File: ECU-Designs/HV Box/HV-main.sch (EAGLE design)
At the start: 62 parts, among them IC2 MCP6002, IC3 MCP6002, T1 120, T2 120, X1 MINIFIT_5566-8

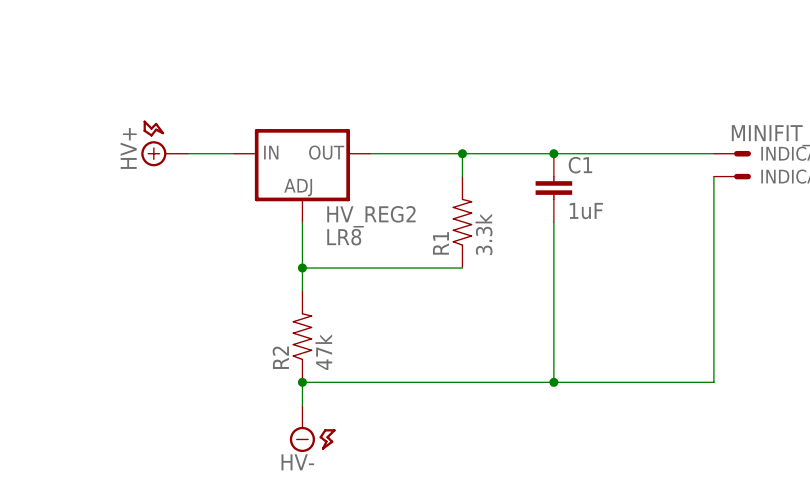
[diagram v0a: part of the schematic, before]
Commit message: Modify elcon charger schematic, fix LR8 values for accumulator indicator for FSAE
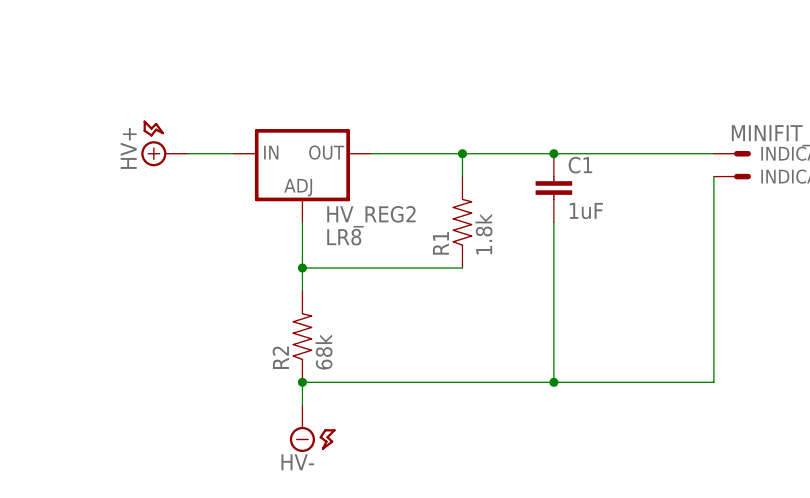
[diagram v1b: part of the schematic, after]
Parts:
- R1: value 3.3k -> 1.8k
- R2: value 47k -> 68k
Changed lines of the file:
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@@
 <?xml version="1.0" encoding="utf-8"?>
 <!DOCTYPE eagle SYSTEM "eagle.dtd">
-<eagle version="7.2.0">
+<eagle version="7.7.0">
 <drawing>
 <settings>
@@
 <setting verticaltext="up"/>
 </settings>
-<grid distance="0.1" unitdist="inch" unit="inch" style="lines" multiple="1" display="no" altdistance="0.05" altunitdist="inch" altunit="inch"/>
+<grid distance="0.1" unitdist="inch" unit="inch" style="lines" multiple="1" display="no" altdistance="0.01" altunitdist="inch" altunit="inch"/>
 <layers>
 <layer number="1" name="Top" color="4" fill="1" visible="no" active="no"/>
@@
 <part name="HV_REG2" library="HyTechDevices" deviceset="HV_LIN_REG_LR8" device="SMD" value="LR8"/>
 <part name="C1" library="HyTechDevices" deviceset="CAP" device="0805" value="1uF"/>
-<part name="R1" library="HyTechDevices" deviceset="RESISTOR" device="0805-RES" value="3.3k"/>
-<part name="R2" library="HyTechDevices" deviceset="RESISTOR" device="0805-RES" value="47k"/>
+<part name="R1" library="HyTechDevices" deviceset="RESISTOR" device="0805-RES" value="1.8k"/>
+<part name="R2" library="HyTechDevices" deviceset="RESISTOR" device="0805-RES" value="68k"/>
 <part name="INDICATOR" library="HyTechDevices" deviceset="MINIFIT_5566-2" device="" value="MINIFIT_5566-2"/>
 <part name="U$6" library="supply2" deviceset="HV+" device=""/>

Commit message: HV Board progress
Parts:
- removed C1, C2: 1uF, HyTechDevices:CAP0805
- removed F1, F2: 2.0, HyTechDevices:RESISTOR0805-RES
- removed FUSE+, FUSE-: 0751.0110_FUSE_CLIP, HyTechDevices:0751.0110_FUSE_CLIP
- removed R3: 6.8k, HyTechDevices:RESISTOR0805-RES
- removed TSMP: MINIFIT_5566-2, HyTechDevices:MINIFIT_5566-2
- removed TSMP_R+, TSMP_R-: 10K, 10w, HyTechDevices:RESISTOR10W
- added FUSE: 250mA, HyTechDevices:FUSE_MIDGET
- added R20: 6.8k, HyTechDevices:RESISTOR0805-RES
- added R21, R22: 500k, HyTechDevices:RESISTOR0805-RES
- added R23, R24: 40k, HyTechDevices:RESISTOR0805-RES
- R5: value 1.5m -> 500k
- R6: value 120k -> 40k
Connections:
- removed net HVIN-: F2.2, HVIN--1.S, HVIN--2.S
- removed net N$31: C2.2, HV_REG1.ADJ, R3.1, R4.2
- removed net N$38: TSMP-1.S, TSMP_R+.2
- removed net N$39: TSMP-2.S, TSMP_R-.2
- removed net N$6: F2.1, FUSE-.1
- removed net N$7: F1.1, FUSE+.1
- new net N$10: R21.1, R22.1
- new net N$11: R21.2, R5.2
- new net N$12: R23.1, R24.1
- new net N$13: R23.2, R6.2
- new net N$9: HV_REG1.ADJ, R20.1, R4.2
- net HV+: now also FUSE.P2, R22.2; no longer FUSE+.2, R5.2, TSMP_R+.1
- net HV-: now also HVIN--1.S, HVIN--2.S; no longer C1.2, FUSE-.2, TSMP_R-.1
- net HVIN+: now also FUSE.P1; no longer F1.2
- net N$1: no longer C1.1
- net N$2: now also R20.2; no longer C2.1, R3.2
- net N$36: now also R24.2; no longer R6.2
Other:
- note added: "IMD Connections"
- note removed: "1/8W 0805 Limiting to 250mA"
- note removed: "IMD & TSMP Connections"

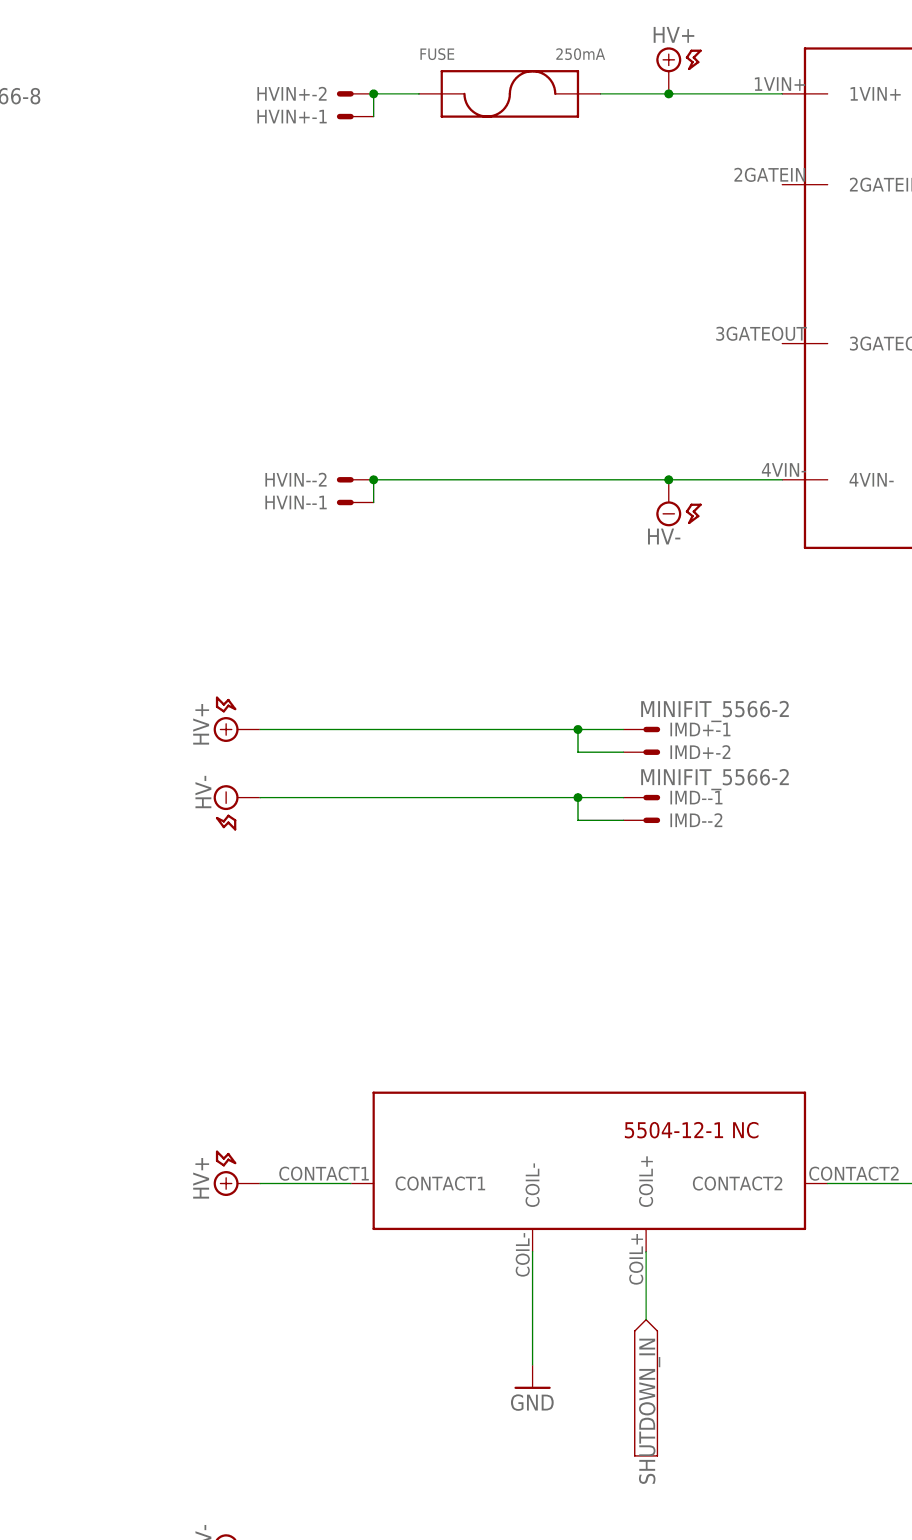
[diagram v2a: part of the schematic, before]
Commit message: Updated HV board and stuffs
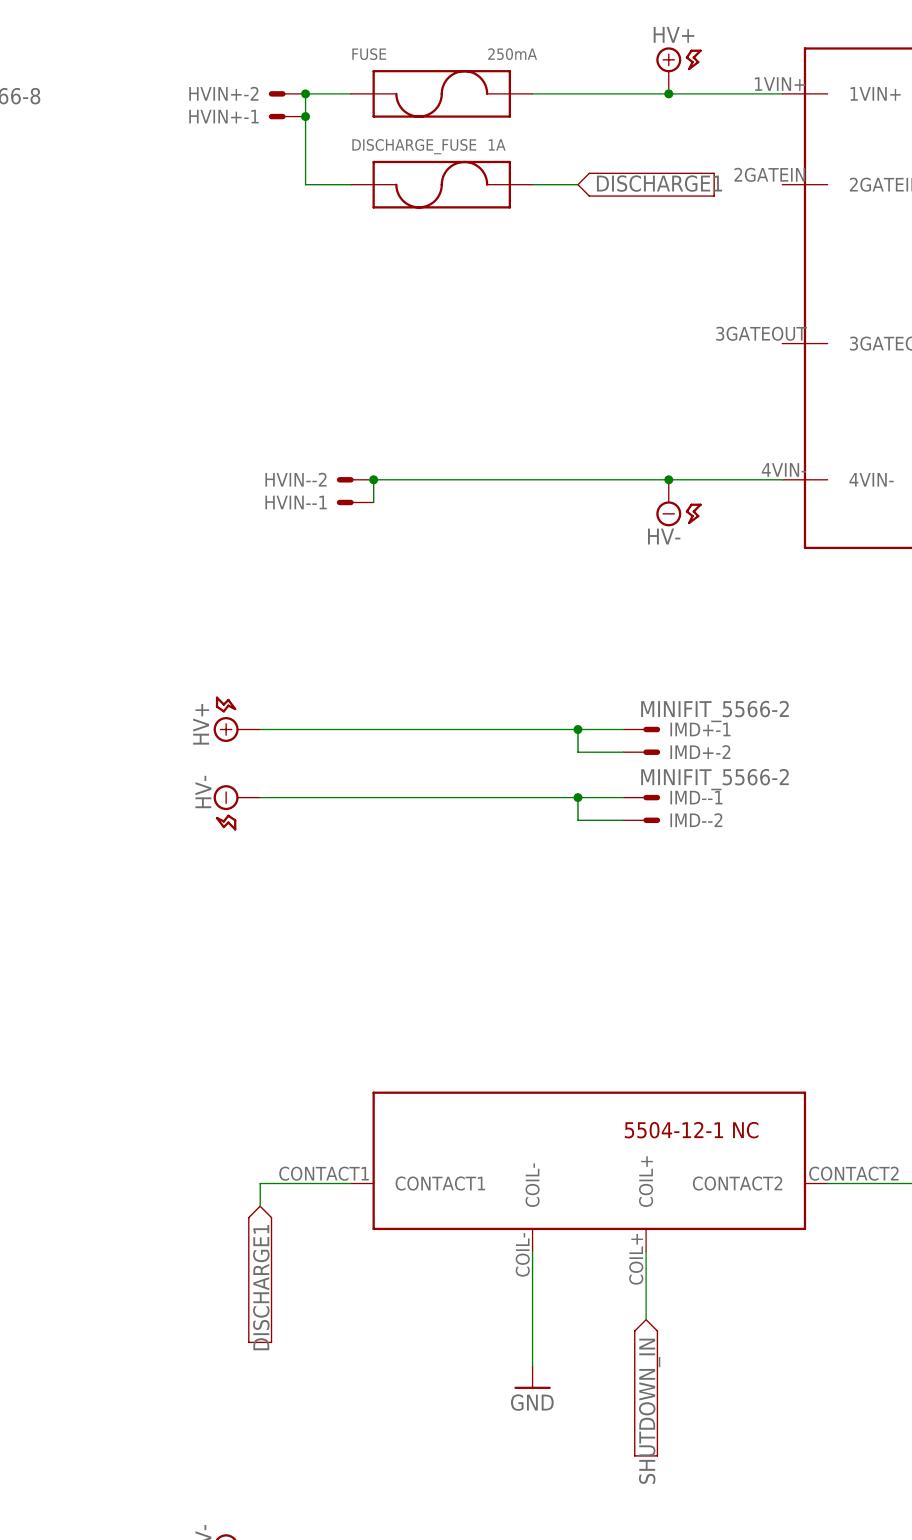
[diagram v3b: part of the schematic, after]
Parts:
- added DISCHARGE_FUSE: 1A, HyTechDevices:FUSE_5X20MM
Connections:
- net N$37 renamed DISCHARGE2
- new net BMS_OK: MAIN-2.S
- new net CHARGE_ENABLE: MAIN-3.S
- new net DISCHARGE1: DISCHARGE_FUSE.P2, U$12.CONTACT1
- net BSPD_CURRENT: now also MAIN-9.S
- net HV+: no longer U$12.CONTACT1
- net HVIN+: now also DISCHARGE_FUSE.P1
- net OKHS_OUT: now also MAIN-1.S
- net SHUTDOWN_IN: now also MAIN-10.S
- net TSAL+: now also MAIN-12.S
- net VDD: now also MAIN-11.S
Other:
- moved on the sheet: FUSE, HVIN+-1, HVIN+-2
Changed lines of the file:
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@@
 <?xml version="1.0" encoding="utf-8"?>
 <!DOCTYPE eagle SYSTEM "eagle.dtd">
-<eagle version="7.2.0">
+<eagle version="8.0.1">
 <drawing>
 <settings>
@@
 <part name="D1" library="HyTechDevices" deviceset="DIODE" device="0805" value=""/>
 <part name="D2" library="HyTechDevices" deviceset="DIODE" device="0805" value=""/>
-<part name="U$4" library="supply2" deviceset="HV+" device=""/>
 <part name="U$14" library="supply2" deviceset="HV-" device=""/>
 <part name="IC3" library="HyTechDevices" deviceset="MCP6002" device=""/>
@@
 <part name="R23" library="HyTechDevices" deviceset="RESISTOR" device="0805-RES" value="40k"/>
 <part name="R24" library="HyTechDevices" deviceset="RESISTOR" device="0805-RES" value="40k"/>
+<part name="SUPPLY17" library="supply2" deviceset="V&lt;--" device="" value="DISCHARGE1"/>
+<part name="DISCHARGE_FUSE" library="HyTechDevices" deviceset="FUSE" device="_5X20MM" value="1A"/>
+<part name="SUPPLY18" library="supply2" deviceset="V&lt;--" device="" value="DISCHARGE1"/>
 </parts>
 <sheets>
@@
 <instance part="SUPPLY1" gate="G$1" x="55.88" y="22.86"/>
 <instance part="SUPPLY3" gate="G$1" x="55.88" y="25.4"/>
-<instance part="HVIN+" gate="-2" x="198.12" y="45.72" rot="R180"/>
-<instance part="HVIN+" gate="-1" x="198.12" y="43.18" rot="R180"/>
+<instance part="HVIN+" gate="-2" x="190.5" y="45.72" rot="R180"/>
+<instance part="HVIN+" gate="-1" x="190.5" y="43.18" rot="R180"/>
 <instance part="HVIN-" gate="-2" x="198.12" y="2.54" rot="R180"/>
 <instance part="HVIN-" gate="-1" x="198.12" y="0" rot="R180"/>
@@
 <instance part="D1" gate="1" x="22.86" y="-187.96" rot="R180"/>
 <instance part="D2" gate="1" x="25.4" y="-203.2" rot="R180"/>
-<instance part="U$4" gate="G$1" x="187.96" y="-76.2" rot="R90"/>
 <instance part="U$14" gate="G$1" x="187.96" y="-116.84" rot="R270"/>
 <instance part="IC3" gate="G$1" x="15.24" y="-119.38"/>
@@
 <instance part="GND5" gate="1" x="86.36" y="50.8" rot="R180"/>
 <instance part="SUPPLY16" gate="G$1" x="55.88" y="30.48"/>
-<instance part="FUSE" gate="G$1" x="215.9" y="45.72"/>
+<instance part="FUSE" gate="G$1" x="208.28" y="45.72"/>
 <instance part="R20" gate="G$1" x="233.68" y="-147.32" rot="R90"/>
 <instance part="R21" gate="G$1" x="236.22" y="-160.02"/>
@@
 <instance part="R23" gate="G$1" x="238.76" y="-172.72" rot="R90"/>
 <instance part="R24" gate="G$1" x="231.14" y="-172.72" rot="R90"/>
+<instance part="SUPPLY17" gate="G$1" x="238.76" y="35.56"/>
+<instance part="DISCHARGE_FUSE" gate="G$1" x="208.28" y="35.56"/>
+<instance part="SUPPLY18" gate="G$1" x="187.96" y="-93.98" rot="R270"/>
 </instances>
 <busses>
@@
 <wire x1="12.7" y1="27.94" x2="40.64" y2="27.94" width="0.1524" layer="91"/>
 <label x="15.24" y="27.94" size="1.778" layer="95"/>
+<pinref part="MAIN" gate="-10" pin="S"/>
 </segment>
 <segment>
@@
 <segment>
 <pinref part="U$5" gate="G$1" pin="1VIN+"/>
-<wire x1="226.06" y1="45.72" x2="233.68" y2="45.72" width="0.1524" layer="91"/>
+<wire x1="218.44" y1="45.72" x2="233.68" y2="45.72" width="0.1524" layer="91"/>
 <pinref part="U$7" gate="G$1" pin="HV+"/>
 <wire x1="233.68" y1="45.72" x2="246.38" y2="45.72" width="0.1524" layer="91"/>
@@
 </segment>
 <segment>
-<wire x1="187.96" y1="-76.2" x2="198.12" y2="-76.2" width="0.1524" layer="91"/>
-<pinref part="U$12" gate="G$1" pin="CONTACT1"/>
-<pinref part="U$4" gate="G$1" pin="HV+"/>
-</segment>
-<segment>
 <pinref part="U$13" gate="G$1" pin="HV+"/>
 <pinref part="R22" gate="G$1" pin="2"/>
@@
 <pinref part="HVIN+" gate="-1" pin="S"/>
 <pinref part="HVIN+" gate="-2" pin="S"/>
-<wire x1="200.66" y1="43.18" x2="200.66" y2="45.72" width="0.1524" layer="91"/>
-<wire x1="205.74" y1="45.72" x2="200.66" y2="45.72" width="0.1524" layer="91"/>
-<junction x="200.66" y="45.72"/>
+<wire x1="193.04" y1="43.18" x2="193.04" y2="45.72" width="0.1524" layer="91"/>
+<wire x1="198.12" y1="45.72" x2="193.04" y2="45.72" width="0.1524" layer="91"/>
+<junction x="193.04" y="45.72"/>
 <pinref part="FUSE" gate="G$1" pin="P1"/>
+<wire x1="193.04" y1="35.56" x2="193.04" y2="43.18" width="0.1524" layer="91"/>
+<junction x="193.04" y="43.18"/>
+<pinref part="DISCHARGE_FUSE" gate="G$1" pin="P1"/>
+<wire x1="193.04" y1="35.56" x2="198.12" y2="35.56" width="0.1524" layer="91"/>
 </segment>
 </net>
@@
 <wire x1="12.7" y1="25.4" x2="40.64" y2="25.4" width="0.1524" layer="91"/>
 <label x="15.24" y="25.4" size="1.778" layer="95"/>
+<pinref part="MAIN" gate="-11" pin="S"/>
 </segment>
 </net>
@@
 <wire x1="12.7" y1="22.86" x2="40.64" y2="22.86" width="0.1524" layer="91"/>
 <label x="15.24" y="22.86" size="1.778" layer="95"/>
+<pinref part="MAIN" gate="-12" pin="S"/>
 </segment>
 <segment>
@@
 </segment>
 </net>
-<net name="N$37" class="0">
+<net name="DISCHARGE2" class="0">
 <segment>
 <pinref part="DISCH1" gate="-1" pin="S"/>
@@
 <wire x1="12.7" y1="50.8" x2="40.64" y2="50.8" width="0.1524" layer="91"/>
 <label x="15.24" y="50.8" size="1.778" layer="95"/>
+<pinref part="MAIN" gate="-1" pin="S"/>
 </segment>
 <segment>
@@
 <wire x1="12.7" y1="48.26" x2="40.64" y2="48.26" width="0.1524" layer="91"/>
 <label x="15.24" y="48.26" size="1.778" layer="95"/>
+<pinref part="MAIN" gate="-2" pin="S"/>
 </segment>
 </net>
@@
 <wire x1="12.7" y1="45.72" x2="40.64" y2="45.72" width="0.1524" layer="91"/>
 <label x="15.24" y="45.72" size="1.778" layer="95"/>
+<pinref part="MAIN" gate="-3" pin="S"/>
 </segment>
 </net>
@@
 <wire x1="40.64" y1="30.48" x2="12.7" y2="30.48" width="0.1524" layer="91"/>
 <label x="15.24" y="30.48" size="1.778" layer="95"/>
+<pinref part="MAIN" gate="-9" pin="S"/>
 </segment>
 </net>
@@
 </segment>
 </net>
+<net name="DISCHARGE1" class="0">
+<segment>
+<pinref part="DISCHARGE_FUSE" gate="G$1" pin="P2"/>
+<wire x1="218.44" y1="35.56" x2="223.52" y2="35.56" width="0.1524" layer="91"/>
+</segment>
+<segment>
+<wire x1="187.96" y1="-76.2" x2="198.12" y2="-76.2" width="0.1524" layer="91"/>
+<pinref part="U$12" gate="G$1" pin="CONTACT1"/>
+<wire x1="187.96" y1="-76.2" x2="187.96" y2="-78.74" width="0.1524" layer="91"/>
+</segment>
+</net>
